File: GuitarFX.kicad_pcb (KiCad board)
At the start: 4 copper layers, 70 x 85 mm, 125 parts, among them IC401 PCM3060PWR, J202 Screw_Terminal_01x02, J301 USB_C_Receptacle_USB2.0, J302 Conn_ARM_SWD_TagConnect_TC2030, J303 Screw_Terminal_01x06, J401 Screw_Terminal_01x02, J402 Screw_Terminal_01x02, SW301 SW_SPDT, U201 NCP718xSN500, U202 NCP1117-3.3_SOT223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

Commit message: Refactoring
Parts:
- C314, C315: value 20p -> 14p
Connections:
- J301 pad S1: (no net) -> unconnected-(J301-SHIELD-PadS1)

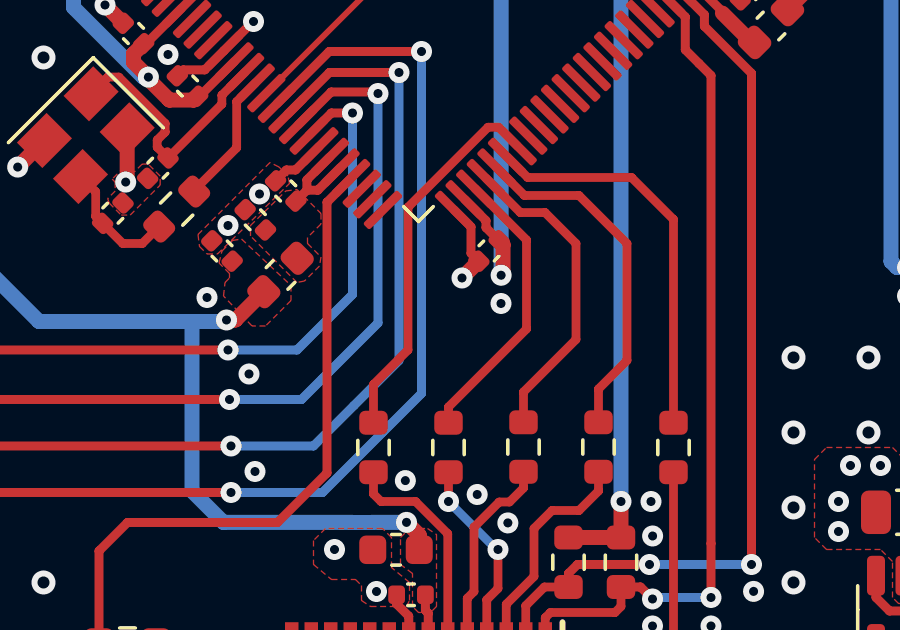
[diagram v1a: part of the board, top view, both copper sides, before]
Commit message: Updated 33R resistors to 0R and changed MCU to H723 from H733
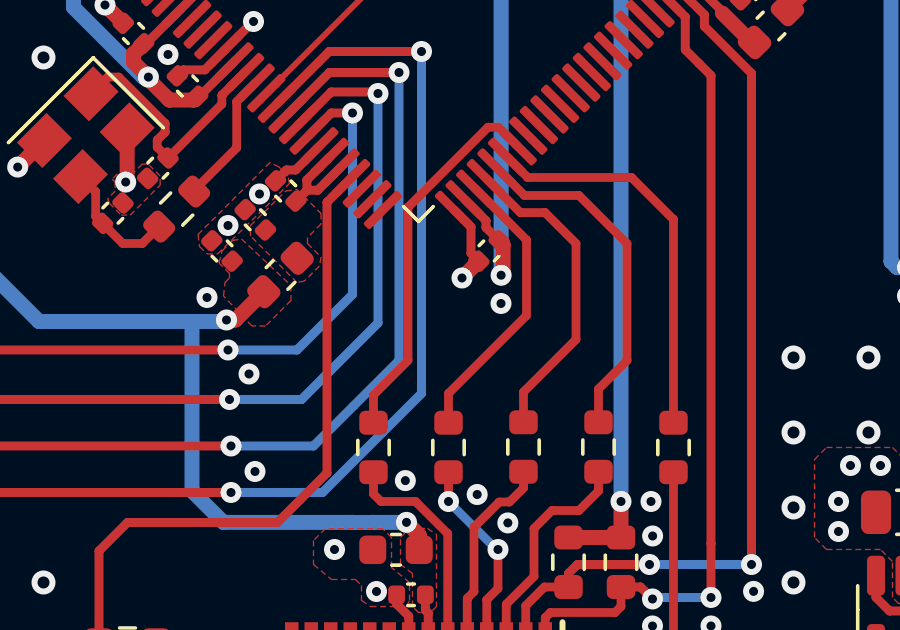
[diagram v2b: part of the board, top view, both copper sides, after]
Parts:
- removed U302: STM32H733VGTx, Package_QFP:LQFP-100_14x14mm_P0.5mm
- added U303: STM32H723VGTx, Package_QFP:LQFP-100_14x14mm_P0.5mm, F.Cu at (145.0, 88.9)
- C314, C315: value 14p -> 10p
- C429, C431, C433: value 0.1u -> 100n
- R302, R305, R306, R307, R308, R419, R420, R424, R426, R428: value 33R -> 0R
- R309, R310: value 325R -> 325R (300R)

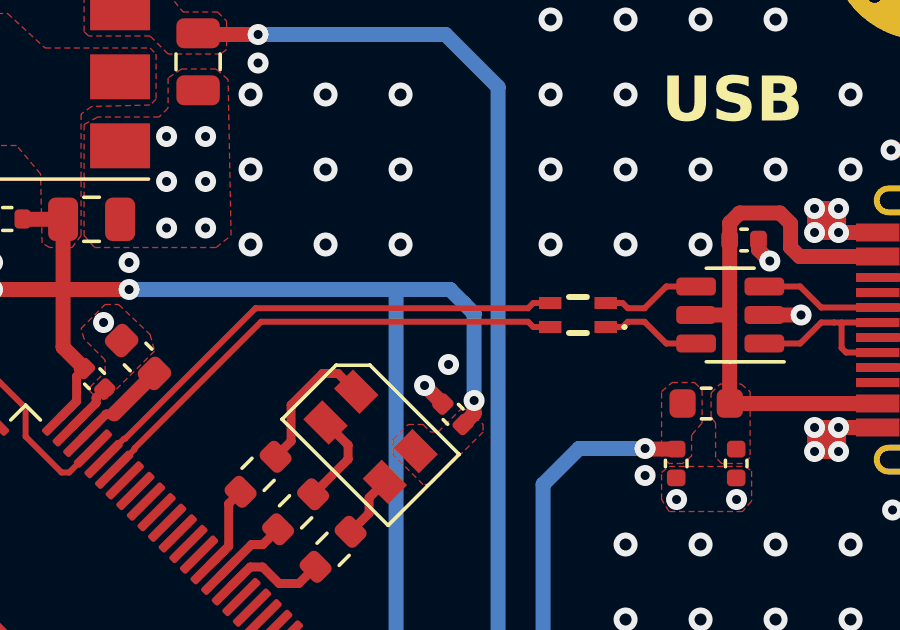
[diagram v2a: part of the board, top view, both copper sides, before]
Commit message: Removed CMC and generated new production files
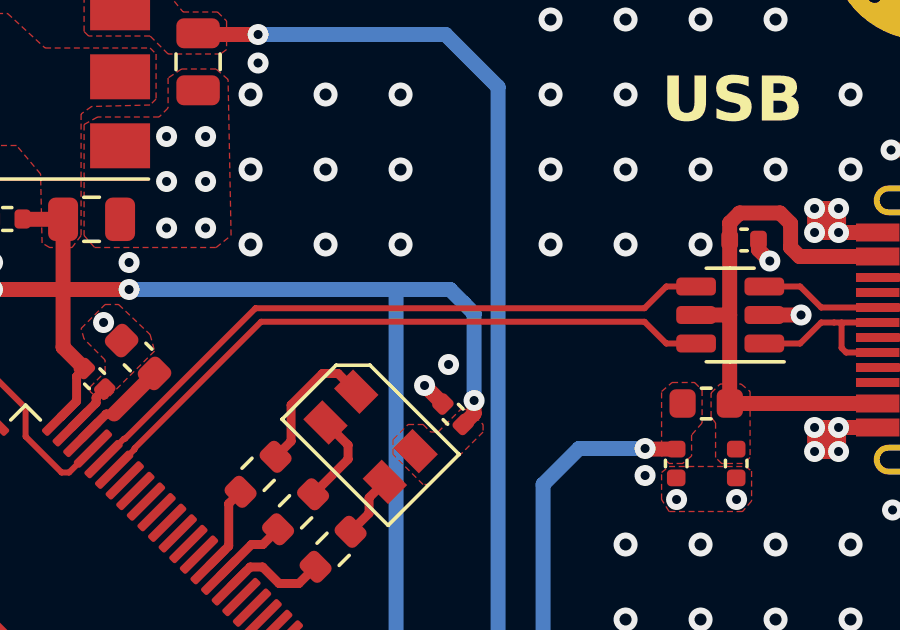
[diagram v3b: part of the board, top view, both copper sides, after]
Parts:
- removed FL301: ACM2012-900-2P-TL002, ACM2012-900-2P-TL002:ACM20129002PTL002
- R405, R421: value 8.2k -> 6.8k
- R406, R422: value 27k -> 22k
- R407, R423: value 15k -> 12k
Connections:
- U301 pad 4: /MCU/USB_CMC_D+ -> /MCU/USB_FS_D+
- U301 pad 6: /MCU/USB_CMC_D- -> /MCU/USB_FS_D-
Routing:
- net /MCU/USB_FS_D+: track 17.0 -> 22.1 mm
- net /MCU/USB_FS_D-: track 16.7 -> 21.8 mm
- net /MCU/USB_CMC_D+: track 3.39 -> 0.00 mm
- net /MCU/USB_CMC_D-: track 3.39 -> 0.00 mm
